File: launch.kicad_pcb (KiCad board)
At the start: 4 copper layers, 298.2 x 113 mm, 271 parts, among them J0 USB_C_Receptacle_USB2.0, U0 USBLC6-2SC6, U1 ATmega32U4-MU, Y0 16Mhz

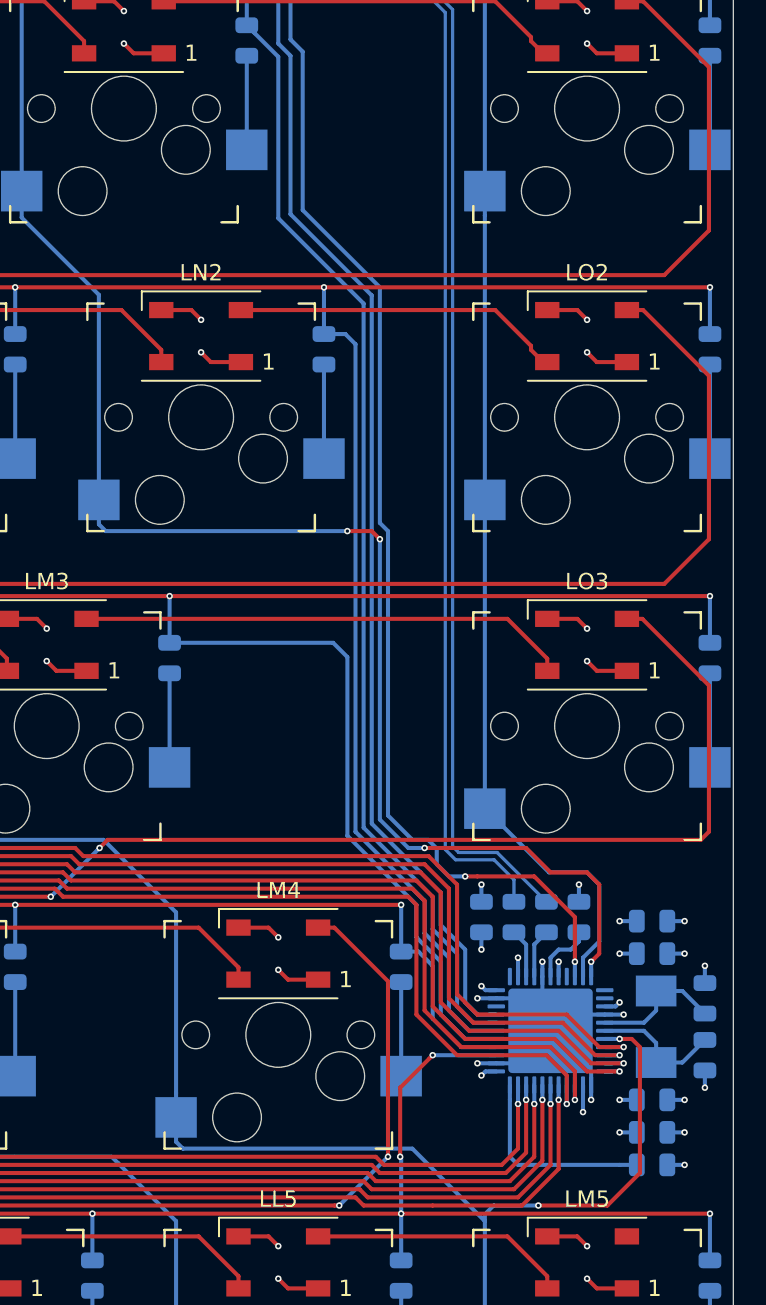
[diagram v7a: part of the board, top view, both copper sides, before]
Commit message: Add ICSP header and add socket model
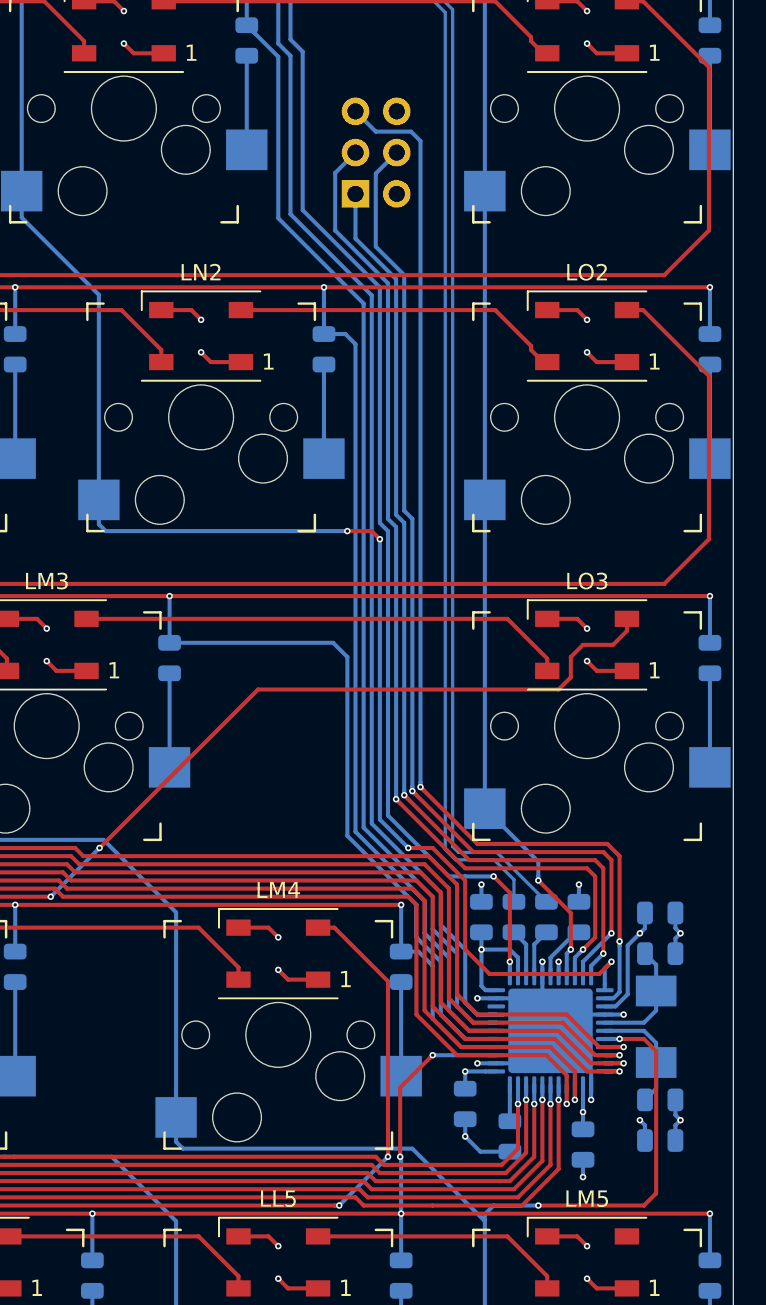
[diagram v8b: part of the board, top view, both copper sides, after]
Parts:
- added J1: AVR-ISP-6, Connector_PinHeader_2.54mm:PinHeader_2x03_P2.54mm_Vertical, B.Cu at (276.0, 34.2)
- SWA0, SWA1, SWA2, SWA3, SWA4, SWA5, SWB0, SWB1, SWB2, SWB3, SWB4, SWB5, SWC0, SWC1, SWC2, SWC3, SWC4, SWC5, SWD0, SWD1, SWD2, SWD3, SWD4, SWD5, SWE0, SWE1, SWE2, SWE3, SWE4, SWE5, SWF0, SWF1, SWF2, SWF3, SWF4, SWG0, SWG1, SWG2, SWG3, SWG4, SWG5, SWH0, SWH1, SWH2, SWH3, SWH4, SWH5, SWI0, SWI1, SWI2, SWI3, SWI4, SWI5, SWJ0, SWJ1, SWJ2, SWJ3, SWJ4, SWJ5, SWK0, SWK1, SWK2, SWK3, SWK4, SWK5, SWL0, SWL1, SWL2, SWL3, SWL4, SWL5, SWM0, SWM1, SWM2, SWM3, SWM4, SWM5, SWN0, SWN1, SWN2, SWO0, SWO1, SWO2, SWO3: footprint keyswitches:Kailh_socket_MX -> Kailh:Kailh_socket_MX
- moved C4 17.6 mm to (294.8, 92.5), turned to 0 degrees
- moved C2 11.6 mm to (282.8, 90.2), turned to 270 degrees
- moved C1 10.5 mm to (283.8, 78.8), turned to 90 degrees
- moved R4 8.92 mm to (285.5, 92.2), turned to 270 degrees
- moved C0 5.06 mm to (290.0, 92.8), turned to 90 degrees
- moved C5 3.89 mm to (294.8, 90.0), turned to 0 degrees
- moved C6 3.89 mm to (294.8, 81.0), turned to 0 degrees
- moved C3 2.55 mm to (294.8, 78.5)
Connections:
- U1 pad 1: Net-(U1-Pad1) -> LED
- U1 pad 10: COLO -> MOSI
- U1 pad 11: COLN -> MISO
- U1 pad 12: Net-(U1-Pad12) -> COLN
- U1 pad 8: Net-(U1-Pad8) -> COLO
- U1 pad 9: LED -> SCLK
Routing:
- net RST: track 0.00 -> 68.0 mm, vias 0 -> 2
- net SCLK: track 0.00 -> 62.8 mm, vias 0 -> 2
- net MOSI: track 0.00 -> 62.7 mm, vias 0 -> 2
- net MISO: track 0.00 -> 59.3 mm, vias 0 -> 2
- net Net-(LA4-Pad4): track 300.6 -> 286.4 mm
- net VCC: track 240.9 -> 251.9 mm, vias 97 -> 92
- net Net-(R4-Pad1): track 12.4 -> 2.22 mm
- net LED: track 356.4 -> 352.7 mm
- net GND: track 271.0 -> 274.4 mm, vias 101 -> 98
- net COLM: track 154.3 -> 156.9 mm
- net COLO: track 72.1 -> 69.6 mm, vias 0 -> 2
- net COLN: track 97.4 -> 99.3 mm
- net Net-(C6-Pad1): track 8.25 -> 7.26 mm
- net Net-(C5-Pad1): track 8.25 -> 7.26 mm
